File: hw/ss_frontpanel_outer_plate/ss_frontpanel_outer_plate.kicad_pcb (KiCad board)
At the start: 2 copper layers, 165 x 51.1 mm, 51 parts, among them J1 Conn_01x04, J2 FFC_conn_14p, M1 NHD3.12-Mechanical_window, M2 Mech_cutout_SS_left_pwrbtn_an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, M3 Mech_cutout_SS_right_rotary_a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, U1 STM32L052C8Tx

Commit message: Updated mech-models of display-board & outer-panel with StepUp. (Had to plot silk-layers as dxf from Kicad to allow StepUp to import them)
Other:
- board text added: "Solderingstation outer frontpanel"
- board text removed: "Solderstation outer frontpanel"
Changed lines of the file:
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@@
   (page A4)
   (layers
-    (0 F.Cu signal)
+    (0 F.Cu signal hide)
     (31 B.Cu power)
     (32 B.Adhes user hide)
@@
   )
   (setup
-    (last_trace_width 0.25)
+    (last_trace_width 0.15)
     (user_trace_width 0.127)
     (user_trace_width 0.15)
@@
       (effects (font (size 0.8 0.7) (thickness 0.15)) (justify mirror))
     )
-    (fp_text user %R (at 0 0) (layer B.Fab)
-      (effects (font (size 0.25 0.25) (thickness 0.04)) (justify mirror))
-    )
     (fp_line (start -0.5 -0.25) (end -0.5 0.25) (layer B.Fab) (width 0.1))
     (fp_line (start -0.5 0.25) (end 0.5 0.25) (layer B.Fab) (width 0.1))
@@
     (fp_line (start 0.93 0.47) (end 0.93 -0.47) (layer B.CrtYd) (width 0.05))
     (fp_line (start 0.93 -0.47) (end -0.93 -0.47) (layer B.CrtYd) (width 0.05))
+    (fp_text user %R (at 0 0) (layer B.Fab)
+      (effects (font (size 0.25 0.25) (thickness 0.04)) (justify mirror))
+    )
     (pad 2 smd roundrect (at 0.485 0) (size 0.59 0.64) (layers B.Cu B.Paste B.Mask) (roundrect_rratio 0.25)
       (net 16 "/Touch-sense controller/HWID"))
@@
       (effects (font (size 0.8 0.7) (thickness 0.15)) (justify mirror))
     )
-    (fp_text user %R (at 0 0 90) (layer B.Fab)
-      (effects (font (size 0.25 0.25) (thickness 0.04)) (justify mirror))
-    )
     (fp_line (start -0.5 -0.25) (end -0.5 0.25) (layer B.Fab) (width 0.1))
     (fp_line (start -0.5 0.25) (end 0.5 0.25) (layer B.Fab) (width 0.1))
@@
     (fp_line (start 0.93 0.47) (end 0.93 -0.47) (layer B.CrtYd) (width 0.05))
     (fp_line (start 0.93 -0.47) (end -0.93 -0.47) (layer B.CrtYd) (width 0.05))
+    (fp_text user %R (at 0 0 90) (layer B.Fab)
+      (effects (font (size 0.25 0.25) (thickness 0.04)) (justify mirror))
+    )
     (pad 2 smd roundrect (at 0.485 0 90) (size 0.59 0.64) (layers B.Cu B.Paste B.Mask) (roundrect_rratio 0.25)
       (net 16 "/Touch-sense controller/HWID"))
@@
       (effects (font (size 0.8 0.7) (thickness 0.15)) (justify mirror))
     )
-    (fp_text user %R (at 0 0) (layer B.Fab)
-      (effects (font (size 0.25 0.25) (thickness 0.04)) (justify mirror))
-    )
     (fp_line (start -0.5 -0.25) (end -0.5 0.25) (layer B.Fab) (width 0.1))
     (fp_line (start -0.5 0.25) (end 0.5 0.25) (layer B.Fab) (width 0.1))
@@
     (fp_line (start 0.93 0.47) (end 0.93 -0.47) (layer B.CrtYd) (width 0.05))
     (fp_line (start 0.93 -0.47) (end -0.93 -0.47) (layer B.CrtYd) (width 0.05))
+    (fp_text user %R (at 0 0) (layer B.Fab)
+      (effects (font (size 0.25 0.25) (thickness 0.04)) (justify mirror))
+    )
     (pad 2 smd roundrect (at 0.485 0) (size 0.59 0.64) (layers B.Cu B.Paste B.Mask) (roundrect_rratio 0.25)
       (net 7 VDD_IO))
@@
     (effects (font (size 2.5 1.5) (thickness 0.375)) (justify mirror))
   )
-  (gr_text "Solderstation outer frontpanel" (at 150 52.7) (layer B.SilkS)
+  (gr_text "Solderingstation outer frontpanel" (at 150 52.7) (layer B.SilkS)
     (effects (font (size 4 1.75) (thickness 0.4)) (justify mirror))
   )
   (gr_line (start 229.4 55.75) (end 227.7 55.75) (layer B.SilkS) (width 0.15))
   (gr_line (start 72.2 55.75) (end 70.5 55.75) (layer B.SilkS) (width 0.15))
-  (gr_line (start 223.7 51.2) (end 170.5 51.2) (layer B.SilkS) (width 0.15))
+  (gr_line (start 223.7 51.2) (end 172.5 51.2) (layer B.SilkS) (width 0.15))
   (gr_line (start 230.4 92.15) (end 230.4 56.75) (layer B.SilkS) (width 0.15))
   (gr_arc (start 227.7 96.15) (end 227.7 93.15) (angle -90) (layer B.SilkS) (width 0.15))
@@
   (gr_line (start 227.7 93.15) (end 229.4 93.15) (layer B.SilkS) (width 0.15))
   (gr_arc (start 223.7 96.7) (end 223.7 97.7) (angle -90) (layer B.SilkS) (width 0.15))
-  (gr_line (start 129.5 51.2) (end 76.2 51.2) (layer B.SilkS) (width 0.15))
+  (gr_line (start 127.5 51.2) (end 76.2 51.2) (layer B.SilkS) (width 0.15))
   (gr_arc (start 72.2 52.75) (end 72.2 55.75) (angle -90) (layer B.SilkS) (width 0.15))
-  (gr_line (start 154.999999 51.200001) (end 149.5 51.200001) (layer B.SilkS) (width 0.15))
+  (gr_line (start 152.999999 51.200001) (end 147 51.200001) (layer B.SilkS) (width 0.15))
   (gr_arc (start 70.5 92.15) (end 69.5 92.15) (angle -90) (layer B.SilkS) (width 0.15))
   (gr_arc (start 229.4 92.15) (end 229.4 93.15) (angle -90) (layer B.SilkS) (width 0.15))

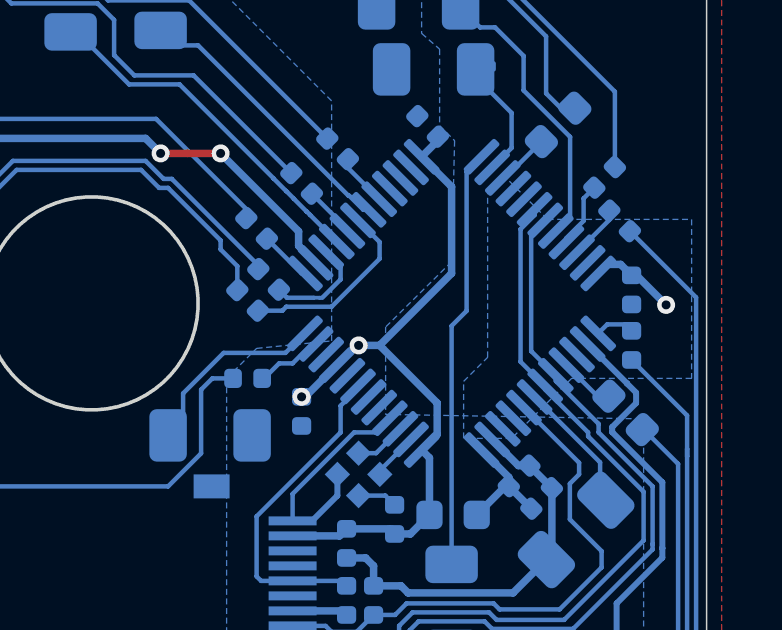
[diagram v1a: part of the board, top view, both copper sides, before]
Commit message: Frontpanel-outer : minor tweaks to align some traces with MCU pads; generated Gerbers
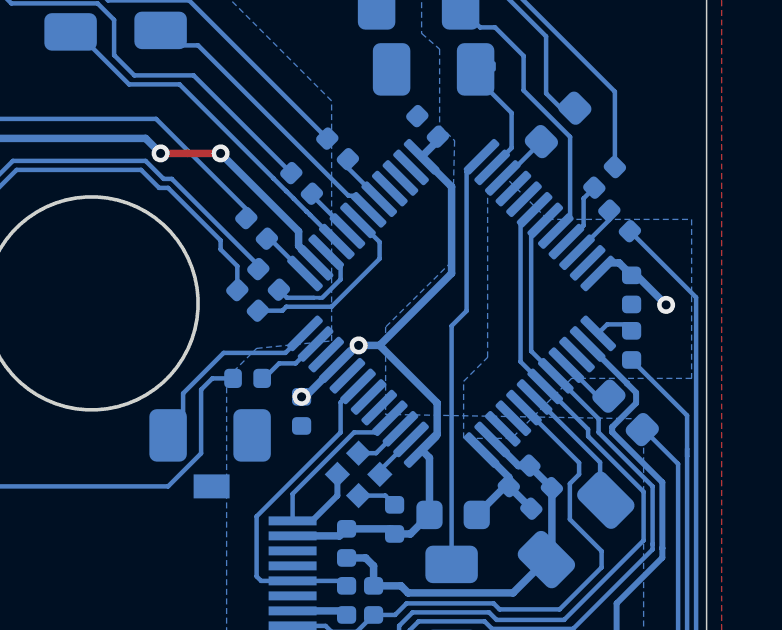
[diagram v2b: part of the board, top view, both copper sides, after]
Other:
- rule pad_to_mask_clearance: 0.05 -> 0

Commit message: Kicad 6.0 : Most of SS2k & subprojects updated to kicad6 The projects should from now on be opened through the .kicad_pro files instead of .pro, etc. NOTE: Kicad 6 is now used. Kicad5 is NOT able to open v6+ files.
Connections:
- net /Touch-sense controller/~AUX_IRQn~ renamed /Touch-sense controller/~{AUX_IRQn}
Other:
- net class Default removed
- net class LTS1_Same removed
- net class LTS2_Same removed
- net class TSC_Others removed

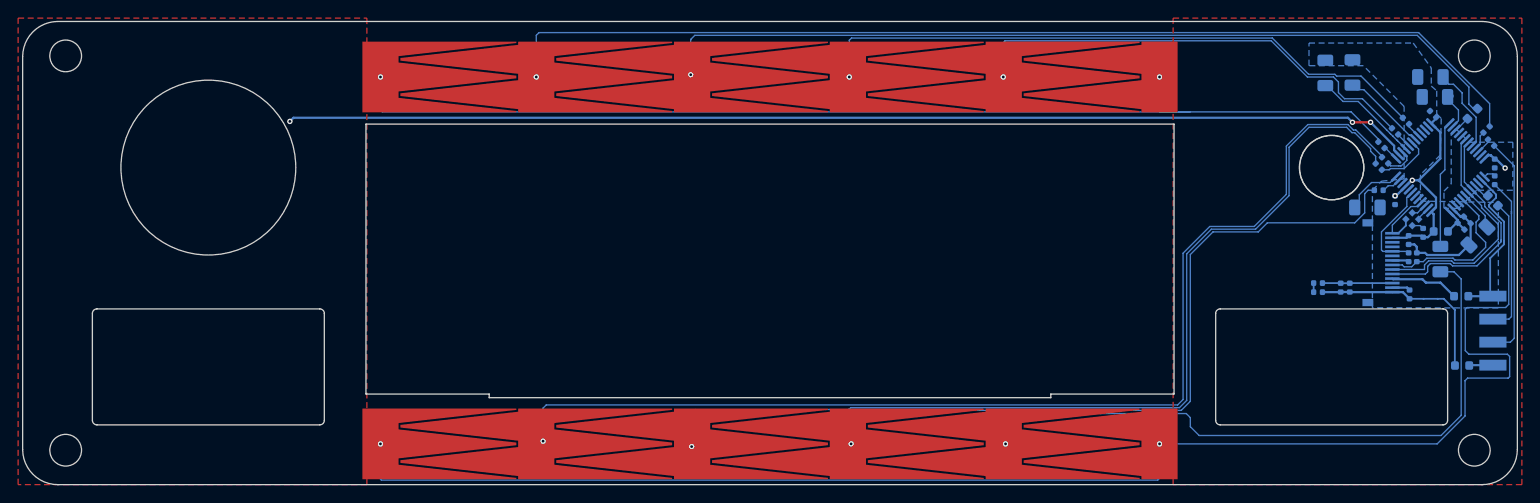
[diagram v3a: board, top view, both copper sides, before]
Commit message: Placeholder 3d-models for rear-panel (w. conns), PSU, Bottom-plate, front-panel (w. conns), outer fp
With these placeholder mech. objects, the build-in 3d view of MB pcb features most of the mechanical
objects that constrain components placements. So 3d-view can be used to quickly check and iterate
placements to avoid 3d collisions, without having to first export MB STEP into FreeCAD and muck around
only to have to repeat again for each iteration
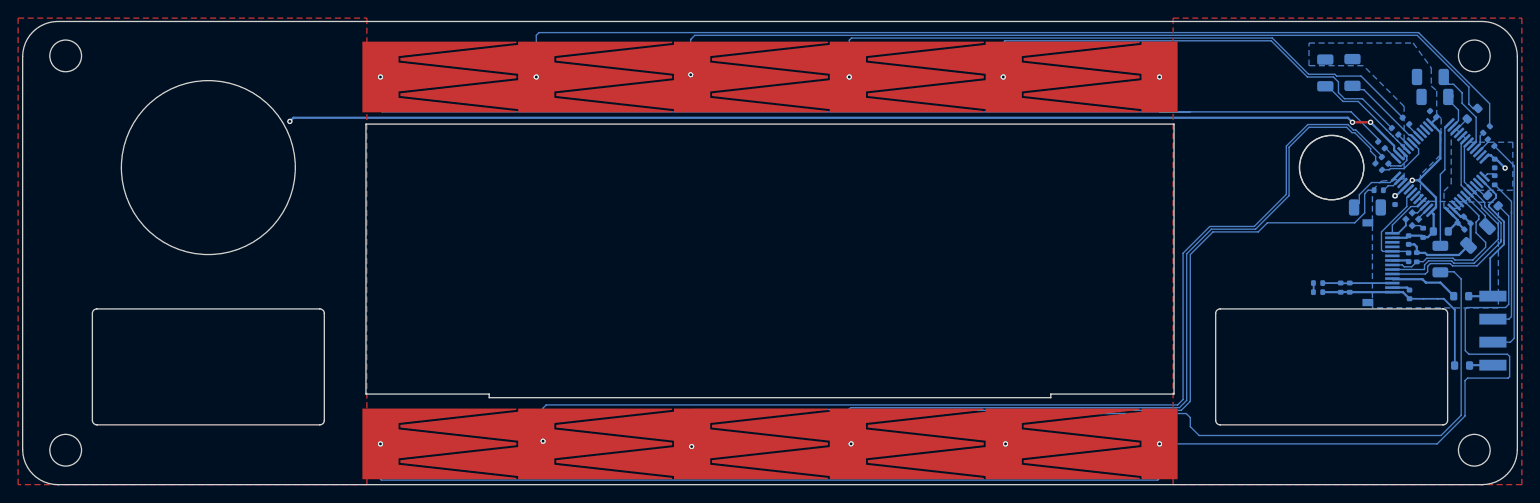
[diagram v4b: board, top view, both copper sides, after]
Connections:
- J2 pad 15: Net-(J2-Pad15) -> unconnected-(J2-Pad15)
- J2 pad 16: Net-(J2-Pad16) -> unconnected-(J2-Pad16)
- U1 pad 29: Net-(U1-Pad29) -> unconnected-(U1-Pad29)
- U1 pad 46: Net-(U1-Pad46) -> unconnected-(U1-Pad46)
- U1 pad 5: Net-(U1-Pad5) -> unconnected-(U1-Pad5)
- U1 pad 6: Net-(U1-Pad6) -> unconnected-(U1-Pad6)

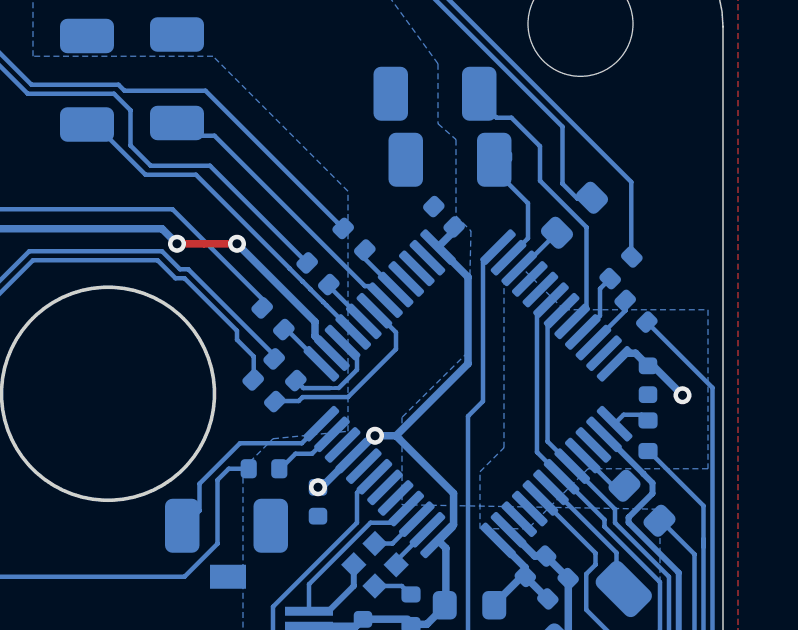
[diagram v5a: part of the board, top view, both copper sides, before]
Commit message: Various boards & schematics (auto-)updated to Kicad-v8
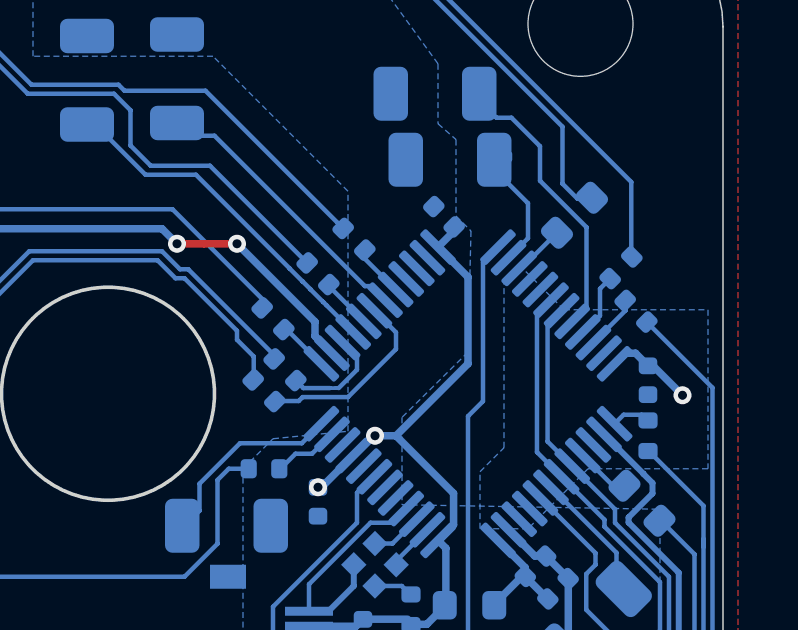
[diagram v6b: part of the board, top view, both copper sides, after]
